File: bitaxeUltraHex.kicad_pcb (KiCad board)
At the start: 4 copper layers, 136.3 x 79.7 mm, 274 parts, among them J1 Conn_01x01, J2 Conn_01x01, J4 TC2030-IDC, J5 Conn_01x04, J6 Conn_01x04, J7 USB_C_Receptacle_USB2.0, Q1 NTMFS5C673NLT1G, Q2 CSD17577Q5A, Q3 NTMFS5C673NLT1G, Q4 CSD17577Q5A, Q5 S8050, SW1 GT-TC029B-H025-L1N, SW2 GT-TC029B-H025-L1N, U1 uA7805, U10 25MHz, U11 BM1366_mode1, U12 ADP171AUJ-R7, U13 ADP171AUJ-R7, U14 BM1366_mode1, U15 TMP1075, U16 TMP1075, U17 EMC2302, U18 EMC2101, U19 ADP171AUJ-R7, U2 RT9080-33GJ5, U20 ADP171AUJ-R7, U21 BM1366_mode1, U22 BM1366_mode1, U23 ADP171AUJ-R7, U24 ADP171AUJ-R7, U25 BM1366_mode1, U26 BM1366_mode1, U27 176x320_st7789, U3 INA219AIDCNR, U4 TPS40305, U5 DS4432U+, U6 SN74LVC1T45DBVR, U7 SN74LVC1T45DBVR, U8 SN74LVC1T45DBVR, U9 ESP32-S3-WROOM-1, Y1 32.768kHz

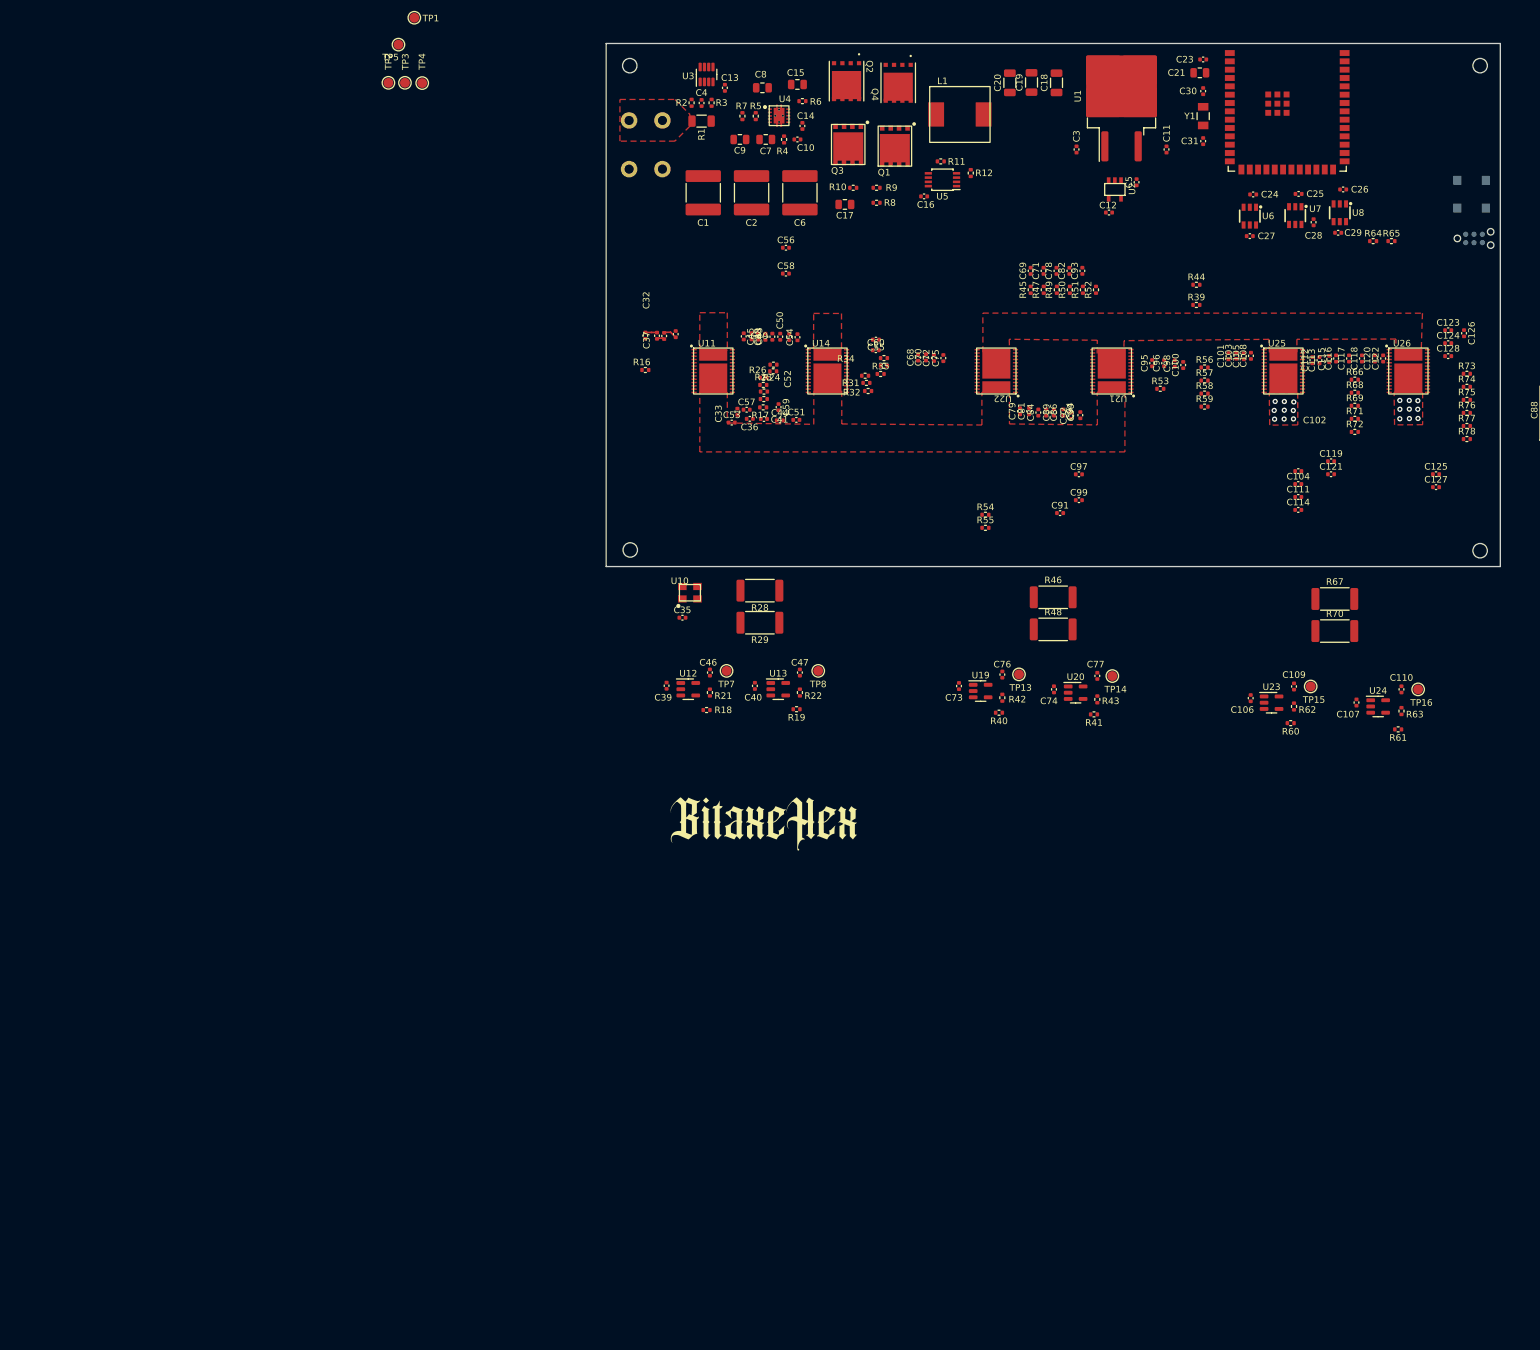
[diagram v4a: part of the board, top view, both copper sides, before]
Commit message: added enclosure edge cuts. added heatsink outline. changed the two middle voltage domain ASICs to mode 0 so the data lines can snake through all 6 chips.
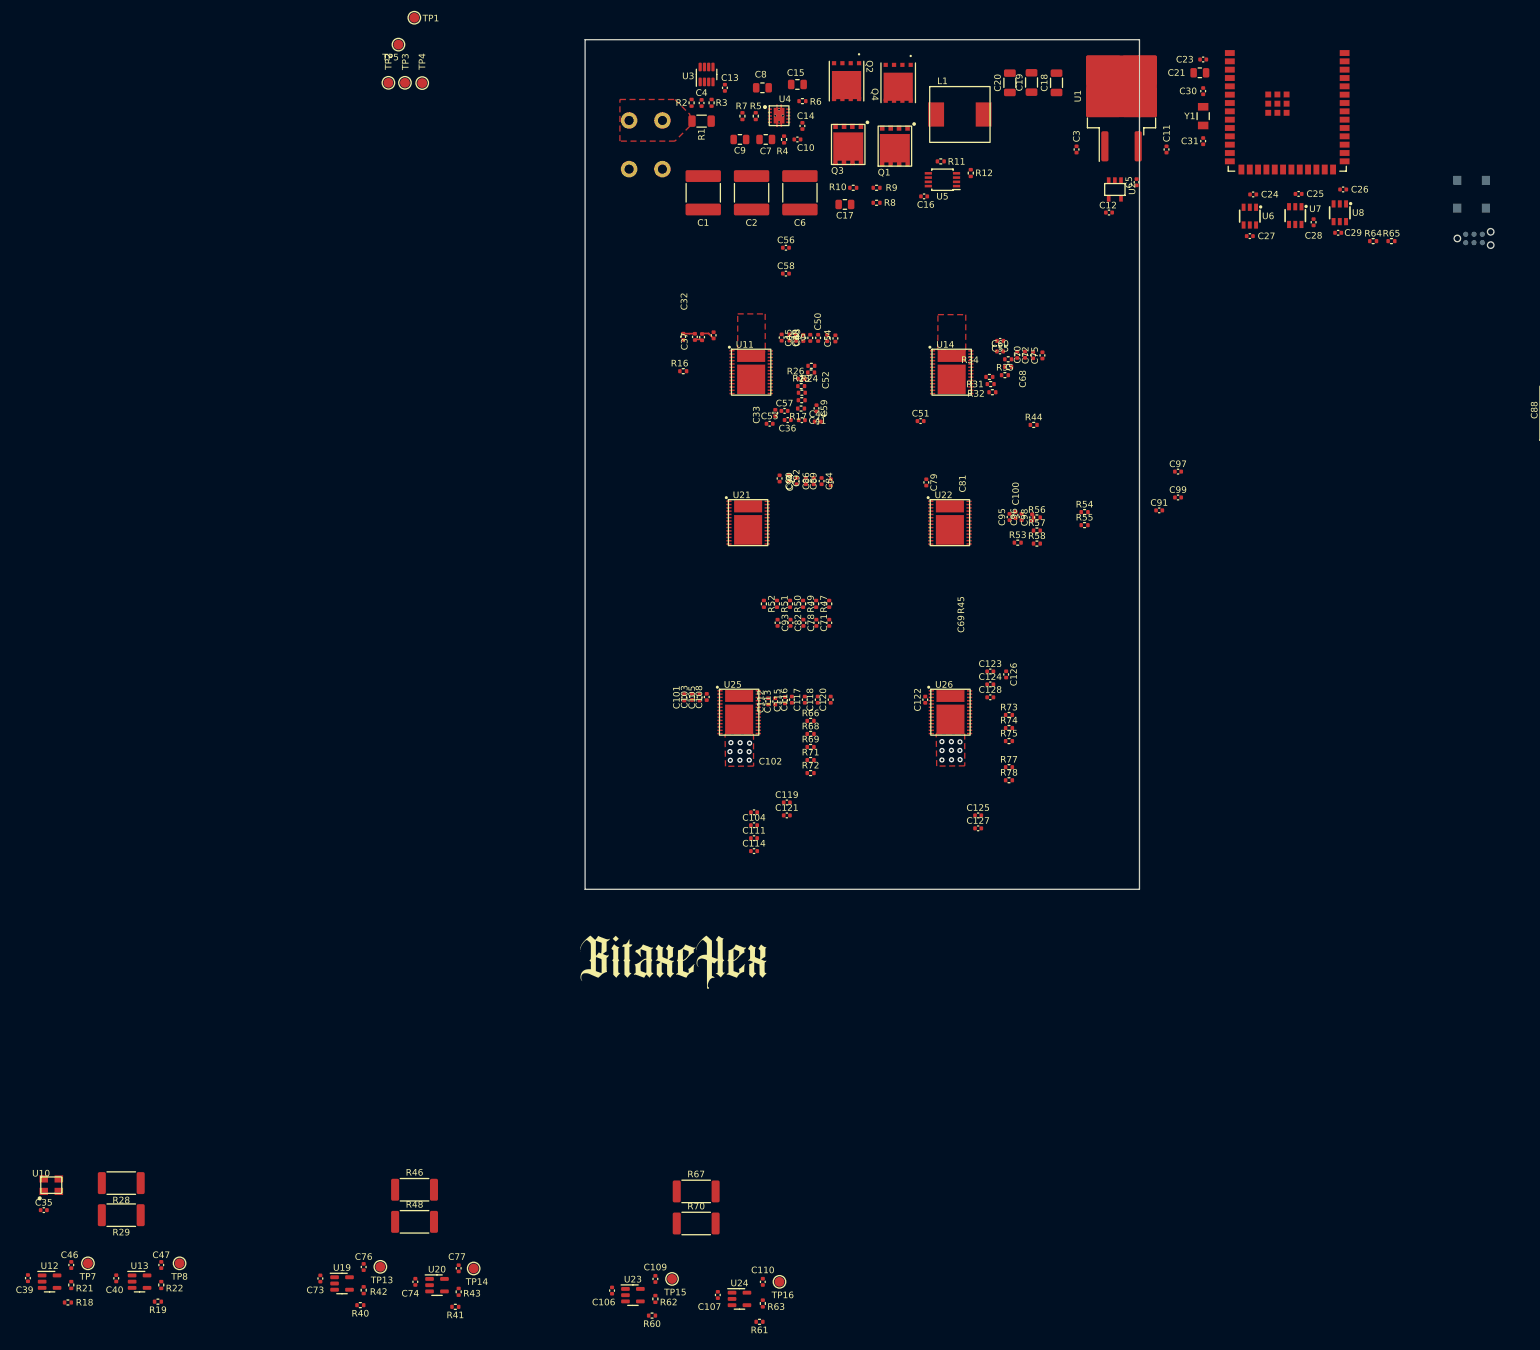
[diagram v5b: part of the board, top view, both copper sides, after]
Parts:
- removed H1, H2, H3, H4: AlignmentHole, MountingHole:MountingHole_2.2mm_M2
- removed R39, R59: 10k, Resistor_SMD:R_0402_1005Metric
- removed R76: 33, Resistor_SMD:R_0402_1005Metric
- moved C110 132.8 mm to (77.4, 236.1)
- moved C40 132.8 mm to (-21.1, 235.6)
- moved C46 132.8 mm to (-28.0, 233.5)
- moved C47 132.8 mm to (-14.3, 233.5)
- moved C74 132.8 mm to (24.4, 236.1)
- moved C77 132.8 mm to (31.0, 234.0)
- moved R18 132.8 mm to (-28.5, 239.2)
- moved R21 132.8 mm to (-28.0, 236.6)
- moved R22 132.8 mm to (-14.3, 236.6)
- moved R43 132.8 mm to (31.0, 237.6)
- moved R48 132.8 mm to (24.3, 227.0)
- moved R62 132.8 mm to (61.0, 238.7)
- moved R67 132.8 mm to (67.2, 222.3)
- moved TP13 132.8 mm to (19.1, 233.8)
- moved TP16 132.8 mm to (79.9, 236.1)
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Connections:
- C82 pad 1: Net-(U21-MODE_1) -> Net-(U21-MODE_0)
- C91 pad 1: Net-(U21-MODE_1) -> Net-(U21-MODE_0)
- C99 pad 2: Net-(U22-MODE_1) -> Net-(U22-MODE_0)
- R44 pad 2: Net-(U21-MODE_1) -> Net-(U21-MODE_0)
- R53 pad 1: Net-(U22-NRSTO) (its old number) -> Net-(U21-NRSTO)
- R54 pad 1: Net-(U22-CO) (its old number) -> Net-(U21-CO)
- R55 pad 1: Net-(U22-NC) -> Net-(U22-MODE_0)
- R55 pad 2: Net-(U22-MODE_1) -> Net-(U22-NC)
- R56 pad 1: Net-(U22-BO) (its old number) -> Net-(U21-BO)
- R57 pad 1: Net-(U22-CLKO) (its old number) -> Net-(U21-CLKO)
- R58 pad 1: Net-(U22-RI) (its old number) -> Net-(U21-RI)
- U21 pad 17: Net-(U21-MODE_1) -> unconnected-(U21-MODE_1-Pad17)
- U21 pad 18: unconnected-(U21-MODE_0-Pad18) -> Net-(U21-MODE_0)
- U21 pad 5: /BM1366-2/NRSTI -> Net-(U21-CO)
- U21 pad 6: Net-(U21-BI) (its old number) -> Net-(U21-CLKO)
- U21 pad 7: /BM1366-2/RO -> Net-(U21-RI)
- U21 pad 8: /BM1366-1/CLKO -> Net-(U21-BO)
- U21 pad 9: /BM1366-2/CI -> Net-(U21-NRSTO)
- U22 pad 12: Net-(U21-MODE_1) -> Net-(U21-MODE_0)
- U22 pad 17: Net-(U22-MODE_1) -> unconnected-(U22-MODE_1-Pad17)
- U22 pad 18: unconnected-(U22-MODE_0-Pad18) -> Net-(U22-MODE_0)
- U22 pad 20: Net-(U22-CO) (its old number) -> /BM1366-2/NRSTI
- U22 pad 21: Net-(U22-CLKO) (its old number) -> /BM1366-1/BO
- U22 pad 22: Net-(U22-RI) (its old number) -> /BM1366-2/RO
- U22 pad 23: Net-(U22-BO) (its old number) -> /BM1366-1/CLKO
- U22 pad 24: Net-(U22-NRSTO) (its old number) -> /BM1366-2/CI
- U25 pad 6: Net-(U25-BI) -> /BM1366-2/BO
- U26 pad 23: Net-(U26-BO) -> unconnected-(U26-BO-Pad23)
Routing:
- removed copper zone on F.Cu, net /FGND1
- removed copper zone on F.Cu, net /FGND2
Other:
- board size 136.3 x 79.7 mm -> 84.5 x 129.5 mm
- board text added: "heatsink footprint"

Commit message: value label cleanup
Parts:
- U21, U22: value BM1366_mode1 -> BM1366_mode0
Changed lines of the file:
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@@
         (effects (font (size 1 1) (thickness 0.15)))
     )
-    (fp_text value "BM1366_mode1" (at 0.07 4.58 unlocked) (layer "F.Fab")
+    (fp_text value "BM1366_mode0" (at 0.07 4.58 unlocked) (layer "F.Fab")
         (effects (font (size 1 1) (thickness 0.15)))
     )
@@
         (effects (font (size 1 1) (thickness 0.15)))
     )
-    (fp_text value "BM1366_mode1" (at 0.07 4.58 unlocked) (layer "F.Fab")
-        (effects (font (size 1 1) (thickness 0.15)))
-    )
+    (fp_text value "BM1366_mode0" (at 0.07 4.58 unlocked) (layer "F.Fab")
+        (effects (font (size 1 1) (thickness 0.15)))
+    )

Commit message: Rough parts placement
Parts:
- removed the C24 at (152.1, 70.4)
- removed the C25 at (159.1, 70.3)
- removed the C28 at (161.4, 74.6)
- removed the C29 at (165.1, 76.2)
- removed the R36 at (217.8, 53.3)
- removed the U6 at (151.6, 73.7)
- removed the U8 at (165.4, 73.2)
- added C102: 0.1uF, Capacitor_SMD:C_0402_1005Metric, F.Cu at (143.0, 145.0)
- added C103: 1uF, Capacitor_SMD:C_0402_1005Metric, F.Cu at (143.0, 147.6)
- added C111: 1uF, Capacitor_SMD:C_0402_1005Metric, F.Cu at (35.1, 159.6)
- added C117: 1uF, Capacitor_SMD:C_0402_1005Metric, F.Cu at (37.1, 159.6)
- added C127: 1uF, Capacitor_SMD:C_0402_1005Metric, F.Cu at (39.1, 159.6)
- added C131: 1uF, Capacitor_SMD:C_0402_1005Metric, F.Cu at (41.0, 159.6)
- added C136: 0.1uF, Capacitor_SMD:C_0402_1005Metric, F.Cu at (43.0, 159.6)
- added C137: 1uF, Capacitor_SMD:C_0402_1005Metric, F.Cu at (45.0, 159.6)
- added C16: 1uF, Capacitor_SMD:C_0402_1005Metric, B.Cu at (97.5, 75.7)
- added C17: 1uF, Capacitor_SMD:C_0402_1005Metric, B.Cu at (106.4, 74.4)
- added C72: 1uF, Capacitor_SMD:C_0402_1005Metric, F.Cu at (138.3, 144.5)
- added C80: 1uF, Capacitor_SMD:C_0402_1005Metric, F.Cu at (138.1, 147.3)
- added C88: 1uF, Capacitor_SMD:C_0402_1005Metric, F.Cu at (138.1, 149.3)
- added C96: 1uF, Capacitor_SMD:C_0402_1005Metric, F.Cu at (138.1, 151.3)
- added R102: 1K, Resistor_SMD:R_0402_1005Metric, F.Cu at (45.1, 165.4)
- added R103: 1K, Resistor_SMD:R_0402_1005Metric, F.Cu at (35.1, 162.4)
- added R104: 10K, Resistor_SMD:R_0402_1005Metric, F.Cu at (37.1, 162.4)
- added R105: 10K, Resistor_SMD:R_0402_1005Metric, F.Cu at (39.1, 162.4)
- added R106: 1K, Resistor_SMD:R_0402_1005Metric, F.Cu at (41.1, 162.4)
- added R108: 1K, Resistor_SMD:R_0402_1005Metric, F.Cu at (43.1, 162.4)
- added R14: 20K, Resistor_SMD:R_0402_1005Metric, F.Cu at (151.9, 91.4)
- added R44: 1K, Resistor_SMD:R_0402_1005Metric, F.Cu at (162.1, 142.7)
- added R45: 10K, Resistor_SMD:R_0402_1005Metric, F.Cu at (165.9, 142.7)
- added R46: 10K, Resistor_SMD:R_0402_1005Metric, F.Cu at (161.5, 139.2)
- added R50: 1K, Resistor_SMD:R_0402_1005Metric, F.Cu at (164.8, 139.2)
- added R51: 1K, Resistor_SMD:R_0402_1005Metric, F.Cu at (158.5, 144.7)
- added R52: 10K, Resistor_SMD:R_0402_1005Metric, F.Cu at (158.2, 147.6)
- added R53: 10K, Resistor_SMD:R_0402_1005Metric, F.Cu at (158.0, 150.8)
- added R59: 1K, Resistor_SMD:R_0402_1005Metric, F.Cu at (158.5, 141.9)
- added R63: 1K, Resistor_SMD:R_0402_1005Metric, F.Cu at (153.7, 143.0)
- added R64: 10K, Resistor_SMD:R_0402_1005Metric, F.Cu at (153.7, 145.0)
- added R65: 10K, Resistor_SMD:R_0402_1005Metric, F.Cu at (153.7, 147.0)
- added R71: 1K, Resistor_SMD:R_0402_1005Metric, F.Cu at (153.7, 149.0)
- added R72: 1K, Resistor_SMD:R_0402_1005Metric, F.Cu at (149.1, 143.3)
- added R73: 10K, Resistor_SMD:R_0402_1005Metric, F.Cu at (149.1, 145.3)
- added R74: 10K, Resistor_SMD:R_0402_1005Metric, F.Cu at (149.1, 147.3)
- added R75: 1K, Resistor_SMD:R_0402_1005Metric, F.Cu at (149.1, 149.1)
- added R77: 1K, Resistor_SMD:R_0402_1005Metric, F.Cu at (149.3, 152.4)
- added R79: 10K, Resistor_SMD:R_0402_1005Metric, F.Cu at (37.1, 168.3)
- added R80: 10K, Resistor_SMD:R_0402_1005Metric, F.Cu at (39.1, 168.3)
- added R82: 1K, Resistor_SMD:R_0402_1005Metric, F.Cu at (43.1, 168.3)
- added R83: 10K, Resistor_SMD:R_0402_1005Metric, F.Cu at (45.1, 168.3)
- added R84: 10K, Resistor_SMD:R_0402_1005Metric, F.Cu at (35.1, 165.4)
- added R88: 1K, Resistor_SMD:R_0402_1005Metric, F.Cu at (37.1, 165.4)
- added R93: 1K, Resistor_SMD:R_0402_1005Metric, F.Cu at (39.1, 165.4)
- added R94: 10K, Resistor_SMD:R_0402_1005Metric, F.Cu at (41.1, 165.4)
- added R95: 10K, Resistor_SMD:R_0402_1005Metric, F.Cu at (43.1, 165.4)
- added TP1: TestPoint, TestPoint:TestPoint_Pad_D1.0mm, F.Cu at (132.1, 43.9)
- added TP10: TestPoint, TestPoint:TestPoint_Pad_D1.0mm, F.Cu at (146.1, 86.9)
- added TP11: TestPoint, TestPoint:TestPoint_Pad_D1.0mm, F.Cu at (159.0, 84.8)
- added TP12: TestPoint, TestPoint:TestPoint_Pad_D1.0mm, F.Cu at (158.8, 88.4)
- added TP2: TestPoint, TestPoint:TestPoint_Pad_D1.0mm, B.Cu at (106.4, 70.9)
- added TP21: TestPoint, TestPoint:TestPoint_Pad_D1.0mm, F.Cu at (119.4, 93.8)
- added TP22: TestPoint, TestPoint:TestPoint_Pad_D1.0mm, F.Cu at (119.4, 96.6)
- added TP25: TestPoint, TestPoint:TestPoint_Pad_D1.0mm, F.Cu at (121.9, 123.4)
- added TP26: TestPoint, TestPoint:TestPoint_Pad_D1.0mm, F.Cu at (121.9, 126.5)
- added TP27: TestPoint, TestPoint:TestPoint_Pad_D1.0mm, F.Cu at (66.3, 164.6)
- added TP28: TestPoint, TestPoint:TestPoint_Pad_D1.0mm, F.Cu at (68.8, 164.8)
- added TP3: TestPoint, TestPoint:TestPoint_Pad_D1.0mm, B.Cu at (106.7, 78.2)
- added TP31: TestPoint, TestPoint:TestPoint_Pad_D1.0mm, F.Cu at (109.5, 165.6)
- added TP32: TestPoint, TestPoint:TestPoint_Pad_D1.0mm, F.Cu at (112.3, 166.1)
- added TP33: TestPoint, TestPoint:TestPoint_Pad_D1.0mm, F.Cu at (66.0, 133.6)
- added TP34: TestPoint, TestPoint:TestPoint_Pad_D1.0mm, F.Cu at (66.3, 130.8)
- added TP37: TestPoint, TestPoint:TestPoint_Pad_D1.0mm, F.Cu at (66.3, 101.9)
- added TP38: TestPoint, TestPoint:TestPoint_Pad_D1.0mm, F.Cu at (66.5, 104.6)
- added TP39: TestPoint, TestPoint:TestPoint_Pad_D1.5mm, F.Cu at (28.2, 84.9)
- added TP4: TestPoint, TestPoint:TestPoint_Pad_D1.0mm, F.Cu at (112.3, 37.9)
- added TP40: TestPoint, TestPoint:TestPoint_Pad_D1.5mm, F.Cu at (28.2, 88.4)
- added TP41: TestPoint, TestPoint:TestPoint_Pad_D1.5mm, F.Cu at (28.2, 92.0)
- added TP42: TestPoint, TestPoint:TestPoint_Pad_D1.5mm, F.Cu at (28.2, 95.5)
- added TP43: TestPoint, TestPoint:TestPoint_Pad_D1.5mm, F.Cu at (28.2, 99.1)
- added TP5: TestPoint, TestPoint:TestPoint_Pad_D1.0mm, F.Cu at (108.7, 38.1)
- added TP6: TestPoint, TestPoint:TestPoint_Pad_D1.0mm, F.Cu at (45.0, 55.1)
- added TP7: TestPoint, TestPoint:TestPoint_Pad_D1.0mm, F.Cu at (45.0, 58.2)
- added U23: TLV3544, Package_SO:TSSOP-14_4.4x5mm_P0.65mm, F.Cu at (40.6, 150.2)
- added U5: MIC5504, Package_TO_SOT_SMD:SOT-23-5_HandSoldering, B.Cu at (102.6, 75.2)
- C1, C10, C14, C15, C2, C3, C5, C6, C7, C8, C9, L1, Q1, Q2, Q3, Q4, R1, R10, R4, R5, R6, R7, R8, R9, U1, U2, U4, U9: moved to B.Cu
- C12: renamed from C11; moved to B.Cu
- C13: renamed from C12; moved to B.Cu
- C19: renamed from C17; moved to B.Cu
- C20: renamed from C18; moved to B.Cu
- C21: renamed from C19; moved to B.Cu
- C22: renamed from C20; moved to B.Cu
- J4: renamed from J7; moved to B.Cu
- Q5: value S8050 -> BSS123; footprint Package_TO_SOT_SMD:SOT-23-3 -> Package_TO_SOT_SMD:SOT-23
- R78: value 33 -> 1K
- R81: value 10 -> 1K
- TP13: renamed from TP3; footprint TestPoint:TestPoint_Pad_D1.5mm -> TestPoint:TestPoint_Pad_D1.0mm
- TP14: renamed from TP4; footprint TestPoint:TestPoint_Pad_D1.5mm -> TestPoint:TestPoint_Pad_D1.0mm
- TP15: renamed from TP5; footprint TestPoint:TestPoint_Pad_D1.5mm -> TestPoint:TestPoint_Pad_D1.0mm
- TP16: renamed from TP6; footprint TestPoint:TestPoint_Pad_D1.5mm -> TestPoint:TestPoint_Pad_D1.0mm
- TP17: renamed from TP9; footprint TestPoint:TestPoint_Pad_D1.5mm -> TestPoint:TestPoint_Pad_D1.0mm
- TP18: renamed from TP10; footprint TestPoint:TestPoint_Pad_D1.5mm -> TestPoint:TestPoint_Pad_D1.0mm
- TP19: renamed from TP11; footprint TestPoint:TestPoint_Pad_D1.5mm -> TestPoint:TestPoint_Pad_D1.0mm
- TP20: renamed from TP12; footprint TestPoint:TestPoint_Pad_D1.5mm -> TestPoint:TestPoint_Pad_D1.0mm
- TP23: renamed from TP7; footprint TestPoint:TestPoint_Pad_D1.5mm -> TestPoint:TestPoint_Pad_D1.0mm
- TP24: renamed from TP8; footprint TestPoint:TestPoint_Pad_D1.5mm -> TestPoint:TestPoint_Pad_D1.0mm
- TP29: renamed from TP13; footprint TestPoint:TestPoint_Pad_D1.5mm -> TestPoint:TestPoint_Pad_D1.0mm
- TP30: renamed from TP14; footprint TestPoint:TestPoint_Pad_D1.5mm -> TestPoint:TestPoint_Pad_D1.0mm
- TP35: renamed from TP15; footprint TestPoint:TestPoint_Pad_D1.5mm -> TestPoint:TestPoint_Pad_D1.0mm
- TP36: renamed from TP16; footprint TestPoint:TestPoint_Pad_D1.5mm -> TestPoint:TestPoint_Pad_D1.0mm
- TP8: renamed from TP1; footprint TestPoint:TestPoint_Pad_D1.5mm -> TestPoint:TestPoint_Pad_D1.0mm
- TP9: renamed from TP2; footprint TestPoint:TestPoint_Pad_D1.5mm -> TestPoint:TestPoint_Pad_D1.0mm
- U18: value EMC2101 -> TLV3544; footprint Package_SO:TSSOP-8_3x3mm_P0.65mm -> Package_SO:TSSOP-14_4.4x5mm_P0.65mm
- U7: value SN74LVC1T45DBVR -> SN74AVC4T774; footprint lcsc:SOT-23-6_L2.9-W1.6-P0.95-LS2.8-BR -> Package_SO:TSSOP-16_4.4x5mm_P0.65mm
- moved R81 221.3 mm to (41.1, 168.3), turned to 90 degrees
- moved U17 216.4 mm to (147.7, 99.3)
- moved C61 216.2 mm to (144.1, 100.1)
- moved C44 214.4 mm to (141.6, 113.3)
- moved C51 214.4 mm to (148.2, 111.3)
- moved R24 214.4 mm to (147.7, 117.0)
- moved R27 214.4 mm to (148.2, 114.3)
- moved TP23 214.4 mm to (150.7, 111.0)
- moved U14 214.4 mm to (144.9, 113.8)
- moved R35 210.5 mm to (152.2, 105.5)
- moved R34 200.6 mm to (143.3, 105.2)
- moved C45 196.5 mm to (140.7, 124.1)
- moved C52 196.5 mm to (147.5, 122.1)
- moved R25 196.5 mm to (147.0, 127.7)
- moved R28 196.5 mm to (147.5, 125.2)
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- renumbered C97 to C100, C98 to C101, C99 to C104, C100 to C105, C101 to C106, C102 to C107, C103 to C108, C104 to C109, C13 to C11, C105 to C110, C108 to C112, C106 to C113, C107 to C114, C111 to C115, C112 to C116, C113 to C118, C114 to C119, C109 to C120, C110 to C121, C115 to C122, C116 to C123, C117 to C124, C118 to C125, C119 to C126, C120 to C128, C121 to C129, C122 to C130, C123 to C132, C124 to C133, C125 to C134, C126 to C135, C127 to C138, C128 to C139, C16 to C18, C21 to C23, C22 to C24, C23 to C25, C129 to C28, C30 to C29, C31 to C30, C61 to C31, C62 to C32, C63 to C33, C64 to C34, C65 to C35, C66 to C36, C67 to C37, C32 to C38, C33 to C39, C34 to C40, C36 to C41, C37 to C42, C38 to C43, C39 to C44, C40 to C45, C41 to C46, C42 to C47, C43 to C48, C44 to C49, C45 to C50, C46 to C51, C47 to C52, C48 to C53, C49 to C54, C50 to C55, C51 to C56, C52 to C57, C53 to C58, C54 to C59, C55 to C60, C35 to C61, C56 to C62, C57 to C63, C58 to C64, C59 to C65, C60 to C66, C68 to C67, C69 to C68, C70 to C69, C71 to C70, C72 to C71, C75 to C73, C73 to C74, C74 to C75, C78 to C76, C79 to C77, C76 to C78, C77 to C79, C84 to C83, C86 to C84, C89 to C85, C90 to C86, C91 to C87, C92 to C89, C93 to C90, C80 to C91, C94 to C92, C83 to C93, C85 to C94, C87 to C95, C95 to C97, C88 to C98, C96 to C99, D2 to D1, J4 to J3, R71 to R100, R72 to R101, R75 to R107, R14 to R15, R15 to R16, R79 to R18, R80 to R19, R37 to R20, R38 to R21, R16 to R22, R17 to R23, R18 to R24, R19 to R25, R20 to R26, R21 to R27, R22 to R28, R23 to R29, R24 to R30, R25 to R31, R26 to R32, R27 to R33, R28 to R34, R29 to R35, R30 to R36, R31 to R37, R32 to R38, R33 to R39, R34 to R40, R35 to R41, R58 to R42, R53 to R43, R57 to R47, R56 to R48, R54 to R49, R40 to R54, R41 to R55, R42 to R56, R43 to R57, R44 to R58, R45 to R60, R47 to R61, R46 to R62, R49 to R66, R50 to R67, R48 to R68, R51 to R69, R52 to R70, R55 to R76, R64 to R85, R60 to R86, R61 to R87, R62 to R89, R63 to R90, R65 to R91, R66 to R92, R68 to R96, R69 to R97, R67 to R98, R70 to R99, U15 to U10, U16 to U11, U17 to U12, U11 to U13, U12 to U14, U13 to U15, U14 to U16, U10 to U17, U21 to U19, U19 to U20, U20 to U21, U25 to U24, U23 to U25, U24 to U26, U26 to U27, U5 to U6, U27 to U8
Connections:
- net /BM1366-2/BO renamed /BM1366-3/BI
- C100 pad 2: /FGND1 -> /BM1366-1/VDD1
- C109 pad 2: GND -> /BM1366-2/VDD2
- C112 pad 2: /FGND1 -> /VDD
- C113 pad 2: GND -> /BM1366-2/VDD2
- C114 pad 2: GND -> /BM1366-2/VDD2
- C115 pad 2: GND -> /BM1366-2/VDD2
- C116 pad 1: /FGND1 -> /VDD
- C120 pad 2: GND -> /BM1366-2/VDD2
- C121 pad 2: GND -> /BM1366-2/VDD2
- C129 pad 2: GND -> /BM1366-2/VDD2
- C130 pad 2: /FGND1 -> /VDD
- C132 pad 1: /FGND1 -> /VDD
- C134 pad 2: GND -> /BM1366-2/VDD2
- C32 pad 1: unconnected-(C62-Pad1) -> /3V3
- C32 pad 2: unconnected-(C62-Pad2) -> GND
- C33 pad 1: unconnected-(C63-Pad1) -> /3V3
- C33 pad 2: unconnected-(C63-Pad2) -> GND
- C41 pad 2: /FGND2 -> GND
- C43 pad 2: /VDD -> /BM1366-1/VDD1
- C44 pad 2: /FGND2 -> GND
- C45 pad 2: /FGND2 -> GND
- C46 pad 2: /FGND2 -> GND
- C47 pad 1: /VDD -> /BM1366-1/VDD1
- C51 pad 2: /FGND2 -> GND
- C52 pad 2: /FGND2 -> GND
- C58 pad 2: /FGND2 -> GND
- C59 pad 2: /VDD -> /BM1366-1/VDD1
- C60 pad 1: /VDD -> /BM1366-1/VDD1
- C61 pad 1: /FGND2 -> GND
- C63 pad 2: /FGND2 -> GND
- C70 pad 2: /FGND1 -> /BM1366-1/VDD1
- C73 pad 2: /FGND2 -> /BM1366-2/VDD2
- C74 pad 2: /FGND1 -> /BM1366-1/VDD1
- C75 pad 2: /FGND1 -> /BM1366-1/VDD1
- C76 pad 2: /FGND1 -> /BM1366-1/VDD1
- C77 pad 1: /FGND2 -> /BM1366-2/VDD2
- C78 pad 2: /FGND1 -> /BM1366-1/VDD1
- C79 pad 2: /FGND1 -> /BM1366-1/VDD1
- C90 pad 2: /FGND1 -> /BM1366-1/VDD1
- C91 pad 1: /FGND2 -> /BM1366-2/VDD
- C91 pad 2: /FGND1 -> /BM1366-1/VDD1
- C92 pad 2: /FGND2 -> /BM1366-2/VDD2
- C93 pad 1: /FGND2 -> /BM1366-2/VDD
- C93 pad 2: /FGND1 -> /BM1366-1/VDD1
- C94 pad 1: /FGND2 -> /BM1366-2/VDD
- C94 pad 2: /FGND1 -> /BM1366-1/VDD1
- C95 pad 1: /FGND2 -> /BM1366-2/VDD
- C95 pad 2: /FGND1 -> /BM1366-1/VDD1
- C97 pad 1: /FGND2 -> /BM1366-2/VDD2
- C98 pad 1: /FGND2 -> /BM1366-2/VDD
- C98 pad 2: /FGND1 -> /BM1366-1/VDD1
- Q5 pad 1: Net-(Q5-B) -> Net-(Q5-G)
- Q5 pad 2: unconnected-(Q5-E-Pad2) -> GND
- Q5 pad 3: Net-(Q5-C) -> Net-(Q5-D)
- R15 pad 2: Net-(Q5-B) -> Net-(Q5-G)
- R16 pad 1: Net-(Q5-B) -> GND
- R16 pad 2: /3V3 -> /ESP32/TFT_BLK
- R22 pad 1: /FGND2 -> GND
- R24 pad 1: /FGND2 -> GND
- R25 pad 1: /FGND2 -> GND
- R34 pad 1: /VDD -> /BM1366-1/VDD1
- R34 pad 2: /FGND2 -> GND
- R35 pad 1: /VDD -> /BM1366-1/VDD1
- R35 pad 2: /FGND2 -> GND
- R39 pad 2: /BM1366-1/BO -> /BM1366-2/BI
- R54 pad 1: /FGND1 -> /BM1366-1/VDD1
- R55 pad 1: /FGND1 -> /BM1366-1/VDD1
- R62 pad 1: /FGND2 -> /BM1366-2/VDD2
- R62 pad 2: /FGND1 -> /BM1366-1/VDD1
- R68 pad 1: /FGND2 -> /BM1366-2/VDD2
- R68 pad 2: /FGND1 -> /BM1366-1/VDD1
- R78 pad 1: Net-(U26-RI) -> Net-(U23A--)
- R78 pad 2: /BM1366-3/RI -> /BM1366-2/VDD2
- R81 pad 1: Net-(Q5-C) -> /BM1366-3/CI
- R81 pad 2: Net-(U27-LEDK) -> Net-(U23A--)
- R86 pad 1: GND -> /BM1366-2/VDD2
- R87 pad 1: GND -> /BM1366-2/VDD2
- R98 pad 1: /FGND1 -> /VDD
- R98 pad 2: GND -> /BM1366-2/VDD2
- R99 pad 1: /FGND1 -> /VDD
- R99 pad 2: GND -> /BM1366-2/VDD2
- U10 pad 4: unconnected-(U15-A0-Pad4) -> /SDA
- U11 pad 4: unconnected-(U16-A0-Pad4) -> /SCL
- U13 pad 29: /VDD -> /BM1366-1/VDD1
- U13 pad 30: /FGND2 -> GND
- U14 pad 2: /FGND2 -> GND
- U15 pad 2: /FGND2 -> GND
- U16 pad 29: /VDD -> /BM1366-1/VDD1
- U16 pad 30: /FGND2 -> GND
- U17 pad 2: /FGND2 -> GND
- U18 pad 1: /3V3 -> /BM1366-2/CI
- U18 pad 2: unconnected-(U18-DP-Pad2) -> Net-(U18A--)
- U18 pad 3: unconnected-(U18-DN-Pad3) -> Net-(U18A-+)
- U18 pad 4: /Fan/FAN_PWM1 -> /BM1366-2/VDD2
- U18 pad 5: GND -> Net-(U18B-+)
- U18 pad 6: /Fan/FAN_TACH1 -> Net-(U18B--)
- U18 pad 7: /SDA -> /BM1366-2/NRSTI
- U18 pad 8: /SCL -> /BM1366-2/BI
- U19 pad 29: /FGND2 -> /BM1366-2/VDD2
- U19 pad 30: /FGND1 -> /BM1366-1/VDD1
- U20 pad 2: /FGND1 -> /BM1366-1/VDD1
- U21 pad 2: /FGND1 -> /BM1366-1/VDD1
- U22 pad 21: /BM1366-1/BO -> /BM1366-2/BI
- U22 pad 29: /FGND2 -> /BM1366-2/VDD2
- U22 pad 30: /FGND1 -> /BM1366-1/VDD1
- U24 pad 29: /FGND1 -> /VDD
- U24 pad 30: GND -> /BM1366-2/VDD2
- U25 pad 2: GND -> /BM1366-2/VDD2
- U26 pad 2: GND -> /BM1366-2/VDD2
- U27 pad 20: Net-(U26-CO) -> /BM1366-3/CO
- U27 pad 21: Net-(U26-CLKO) -> /BM1366-3/CLKO
- U27 pad 22: Net-(U26-RI) -> /BM1366-3/RI
- U27 pad 23: unconnected-(U26-BO-Pad23) -> /BM1366-3/BO
- U27 pad 24: Net-(U26-NRSTO) -> /BM1366-3/NRSTO
- U27 pad 29: /FGND1 -> /VDD
- U27 pad 30: GND -> /BM1366-2/VDD2
- U7 pad 1: /1V8 -> /3V3
- U7 pad 4: /RO -> /CI
- U7 pad 5: /1V8 -> /NRSTI
- U7 pad 6: /3V3 -> Net-(U7-A4)
- U8 pad 2: Net-(U27-LEDK) -> Net-(Q5-D)
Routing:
- net Net-(U13-VDD1_0): track 2.26 -> 0.01 mm
- net Net-(U13-VDD3_0): track 1.80 -> 0.03 mm
- net Net-(U13-VDD2_0): track 1.01 -> 0.20 mm
- added copper zone on In1.Cu, net (none)
- removed copper zone on F.Cu, net /Power/VIN
- removed copper zone on F.Cu, net /VDD

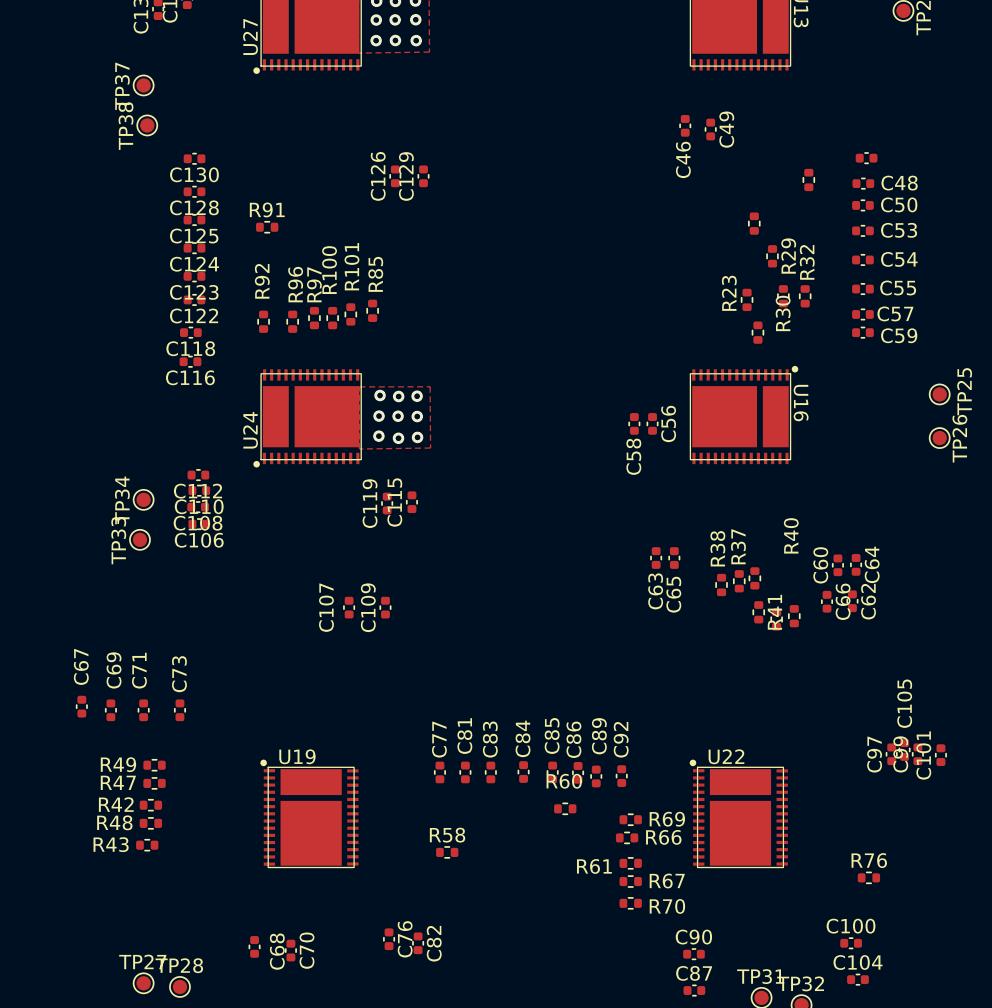
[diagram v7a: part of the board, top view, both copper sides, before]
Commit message: shuffle resistors
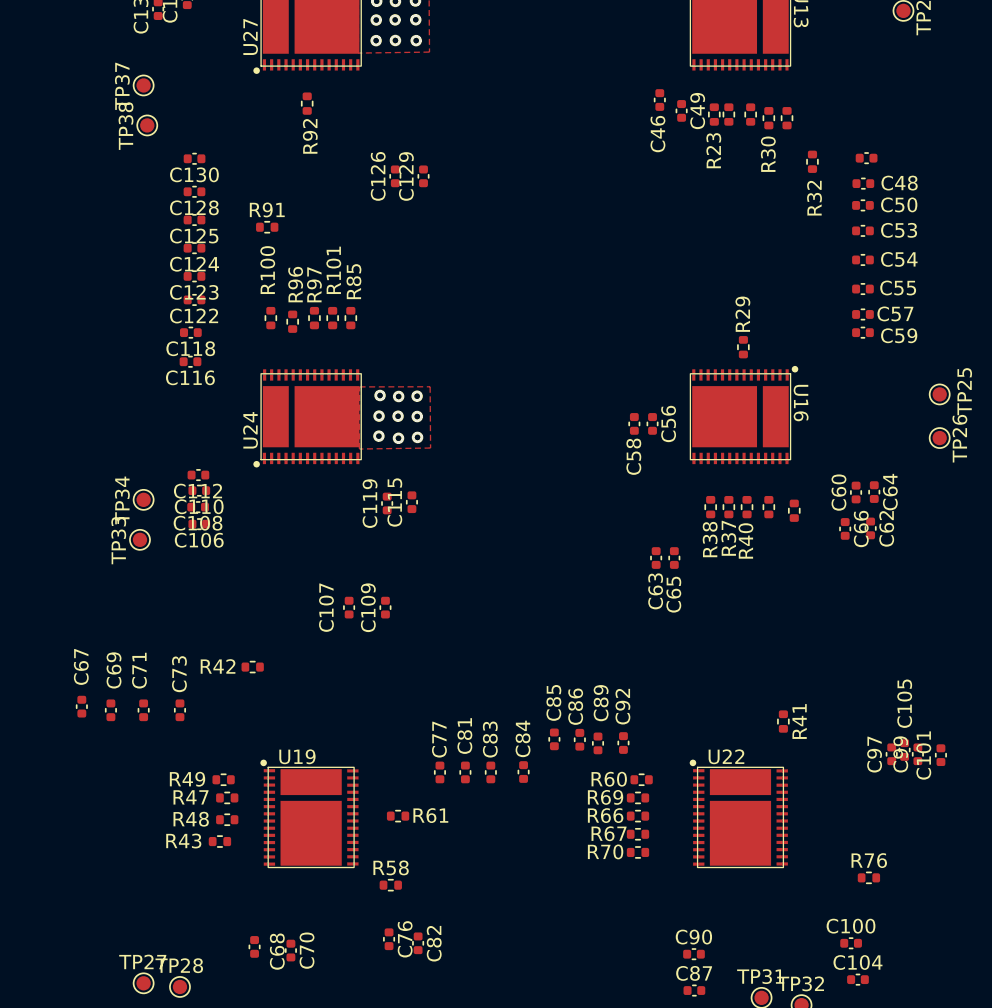
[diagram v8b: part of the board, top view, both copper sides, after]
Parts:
- moved R61 16.6 mm to (84.1, 152.9)
- moved R92 15.5 mm to (77.7, 103.1)
- moved R31 15.2 mm to (108.7, 103.9)
- moved R23 13.2 mm to (106.2, 103.9)
- moved R30 12.5 mm to (110.0, 104.1)
- moved R42 12.0 mm to (73.9, 142.5)
- moved R32 9.41 mm to (113.0, 107.2)
- moved R39 7.87 mm to (110.0, 131.3)
- moved R33 7.83 mm to (107.2, 103.9)
- moved R41 7.83 mm to (111.0, 146.3)
- moved R36 7.37 mm to (111.8, 131.6)
- moved R29 6.67 mm to (108.2, 120.1)
- moved R60 5.71 mm to (101.1, 150.4), turned to 180 degrees
- moved R38 5.49 mm to (105.9, 131.3)
- moved R48 5.34 mm to (72.1, 153.2)
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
